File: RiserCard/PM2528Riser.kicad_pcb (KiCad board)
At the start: 2 copper layers, 90.5 x 105 mm, 65 parts, among them K2 Conn_02x40_Odd_Even

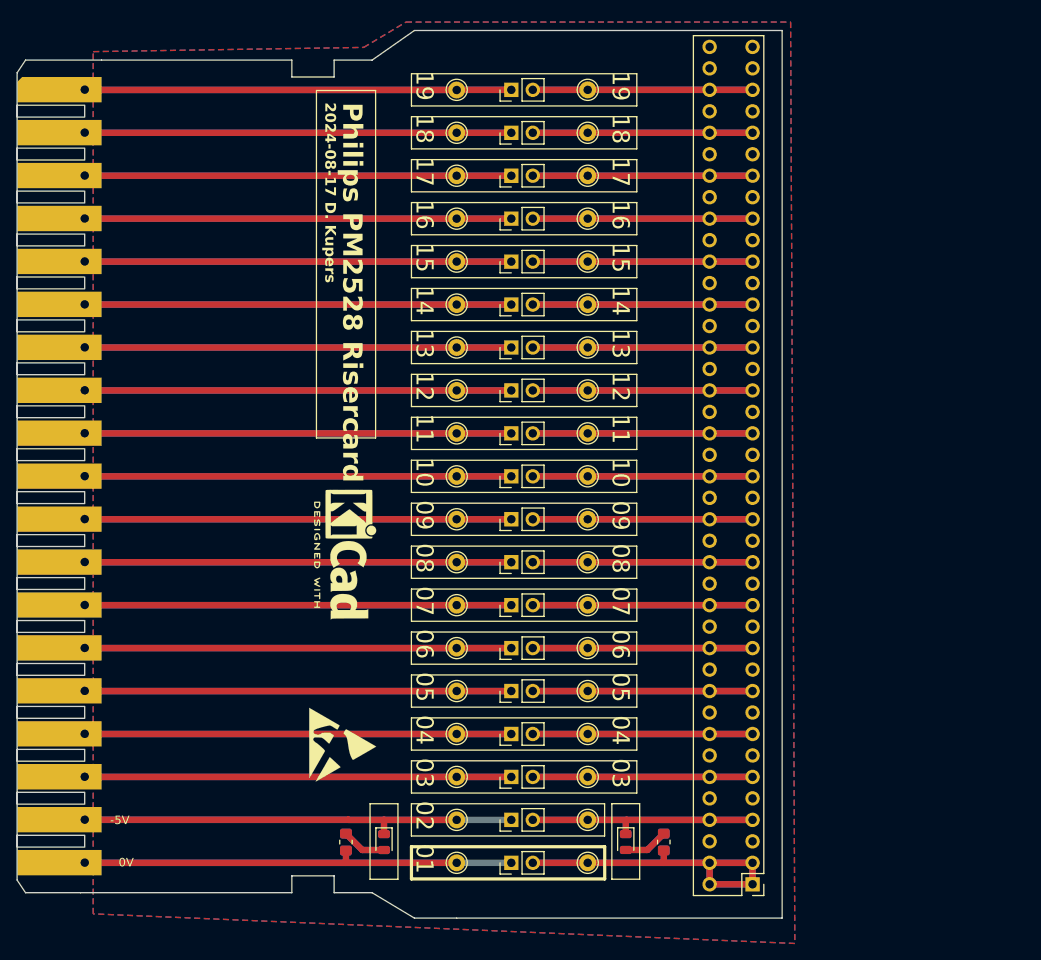
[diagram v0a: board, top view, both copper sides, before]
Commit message: Added new files for N21
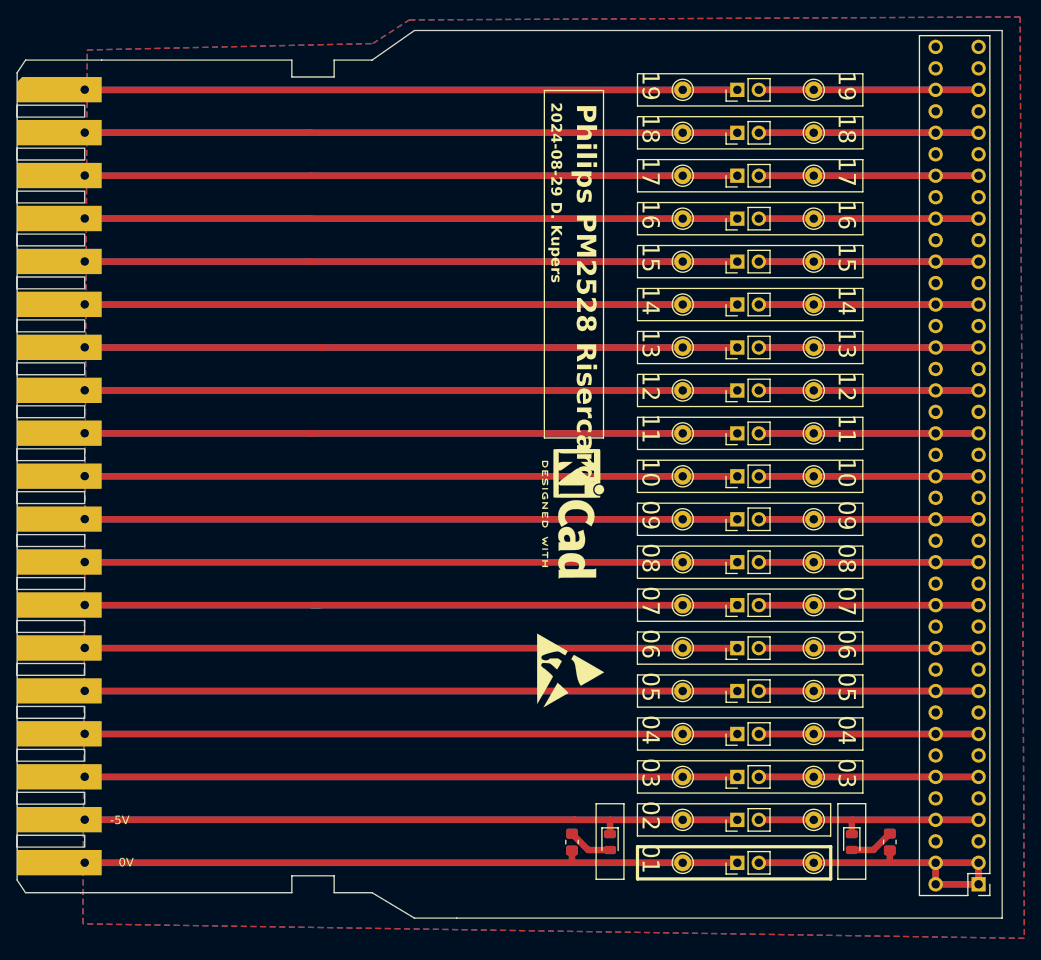
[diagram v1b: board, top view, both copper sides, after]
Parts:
- moved REF** 28.4 mm to (123.5, 108.7)
- moved REF** 27.4 mm to (124.5, 90.2)
- moved D2 26.7 mm to (156.7, 129.0)
- moved K2 26.7 mm to (171.7, 134.0)
- moved R2 26.7 mm to (161.2, 129.0)
- moved TPA01 26.7 mm to (136.7, 131.5)
- moved TPA02 26.7 mm to (136.7, 126.4)
- moved TPA03 26.7 mm to (136.7, 121.3)
- moved TPA04 26.7 mm to (136.7, 116.2)
- moved TPA05 26.7 mm to (136.7, 111.1)
- moved TPA06 26.7 mm to (136.7, 106.1)
- moved TPA07 26.7 mm to (136.7, 101.0)
- moved TPA08 26.7 mm to (136.7, 95.9)
- moved TPA09 26.7 mm to (136.7, 90.8)
- moved TPA10 26.7 mm to (136.7, 85.7)
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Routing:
- net Net-(D1-K): track 96.2 -> 156.1 mm
- net Net-(JP1-A): track 95.9 -> 155.8 mm
- net Net-(JP13-A): track 100.9 -> 155.6 mm
- net Net-(JP7-A): track 100.9 -> 155.6 mm
- net Net-(JP18-A): track 100.9 -> 154.4 mm
- net Net-(JP16-A): track 100.9 -> 154.4 mm
- net Net-(JP9-A): track 100.9 -> 154.4 mm
- net Net-(JP6-A): track 100.9 -> 154.4 mm
- net Net-(JP5-A): track 100.9 -> 154.4 mm
- net Net-(JP4-A): track 100.9 -> 154.4 mm
- net Net-(JP3-A): track 100.9 -> 154.4 mm
- net Net-(JP14-A): track 100.9 -> 154.4 mm
- net Net-(JP12-A): track 100.9 -> 154.4 mm
- net Net-(JP11-A): track 100.9 -> 154.4 mm
- net Net-(JP10-A): track 100.9 -> 154.4 mm
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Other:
- board size 90.5 x 105 mm -> 116.5 x 105 mm
- board text added: "2024-08-29 D. Kupers"
- board text removed: "2024-08-17 D. Kupers"

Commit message: Replaced testpins with testloops/beads
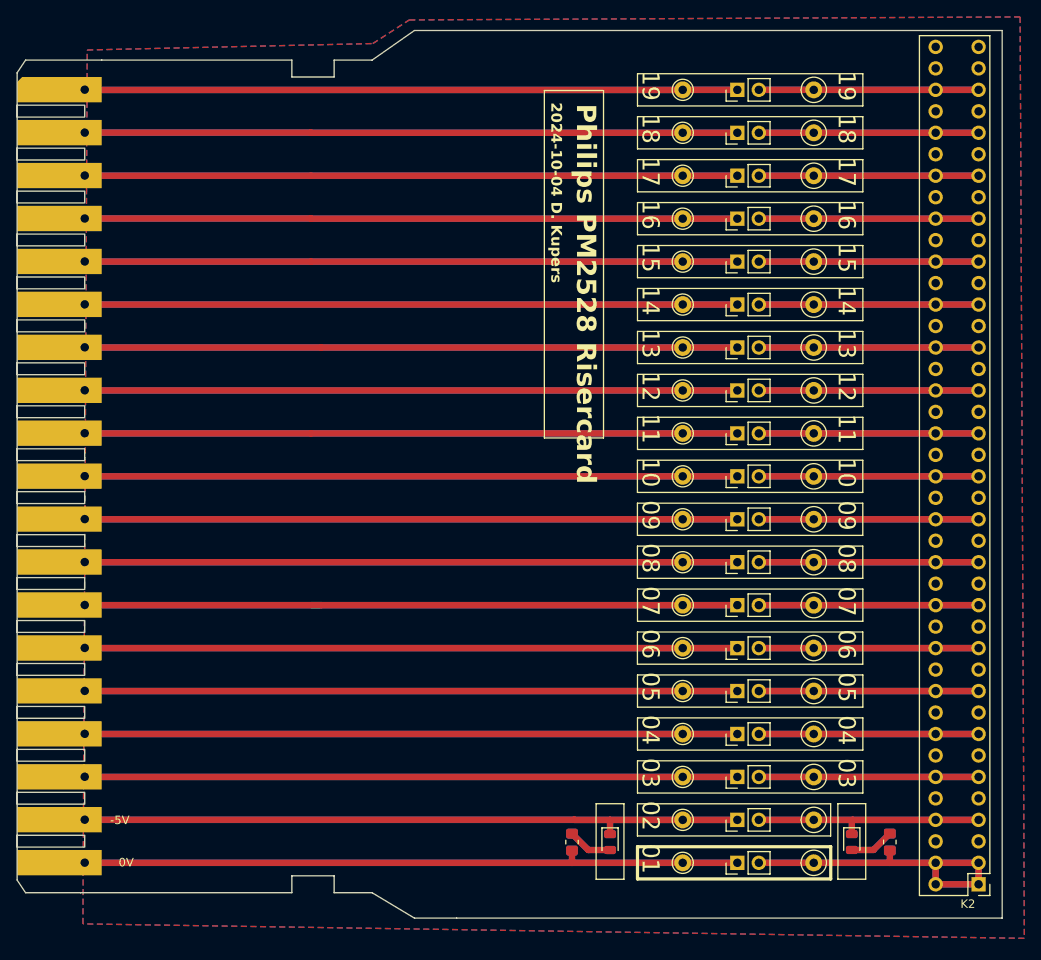
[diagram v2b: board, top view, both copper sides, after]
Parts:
- removed REF**: KiCad-Logo2_6mm_SilkScreen, Symbol:KiCad-Logo2_6mm_SilkScreen
- removed REF**: ESD-Logo_8.9x8mm_SilkScreen, Symbol:ESD-Logo_8.9x8mm_SilkScreen
- TPB01, TPB02, TPB03, TPB04, TPB05, TPB06, TPB07, TPB08, TPB09, TPB10, TPB11, TPB12, TPB13, TPB14, TPB15, TPB16, TPB17, TPB18, TPB19: footprint Connector_Pin:Pin_D1.0mm_L10.0mm -> TestPoint:TestPoint_Loop_D1.80mm_Drill1.0mm_Beaded
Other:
- board text added: "2024-10-04 D. Kupers"
- board text removed: "${REFERENCE}"
- board text removed: "2024-08-29 D. Kupers"

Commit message: Updates, add N25
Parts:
- added REF**: KiCad-Logo2_5mm_SilkScreen, Symbol:KiCad-Logo2_5mm_SilkScreen, F.Cu at (116.5, 75.8)
- K1: footprint Philips_PM2528:PM2528_RiserCardConnector -> PM2528:PM2528_RiserCardConnector
- K2: footprint Philips_PM2528:CONN EDGE DUAL FMALE 80POS 0.100 -> PM2528:CONN EDGE DUAL FMALE 80POS 0.100
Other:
- board text added: "2025-04-04 D. Kupers"
- board text removed: "2024-10-04 D. Kupers"
